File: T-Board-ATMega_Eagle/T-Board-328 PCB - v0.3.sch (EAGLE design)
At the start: 25 parts, among them IC1 LD117MIRROR, IC4 NCP1117MIRROR, J1 POWER_JACKPTH, J2 AVR_SPI_PRG_6PTH, U1 ATMEGA328P_PDIP

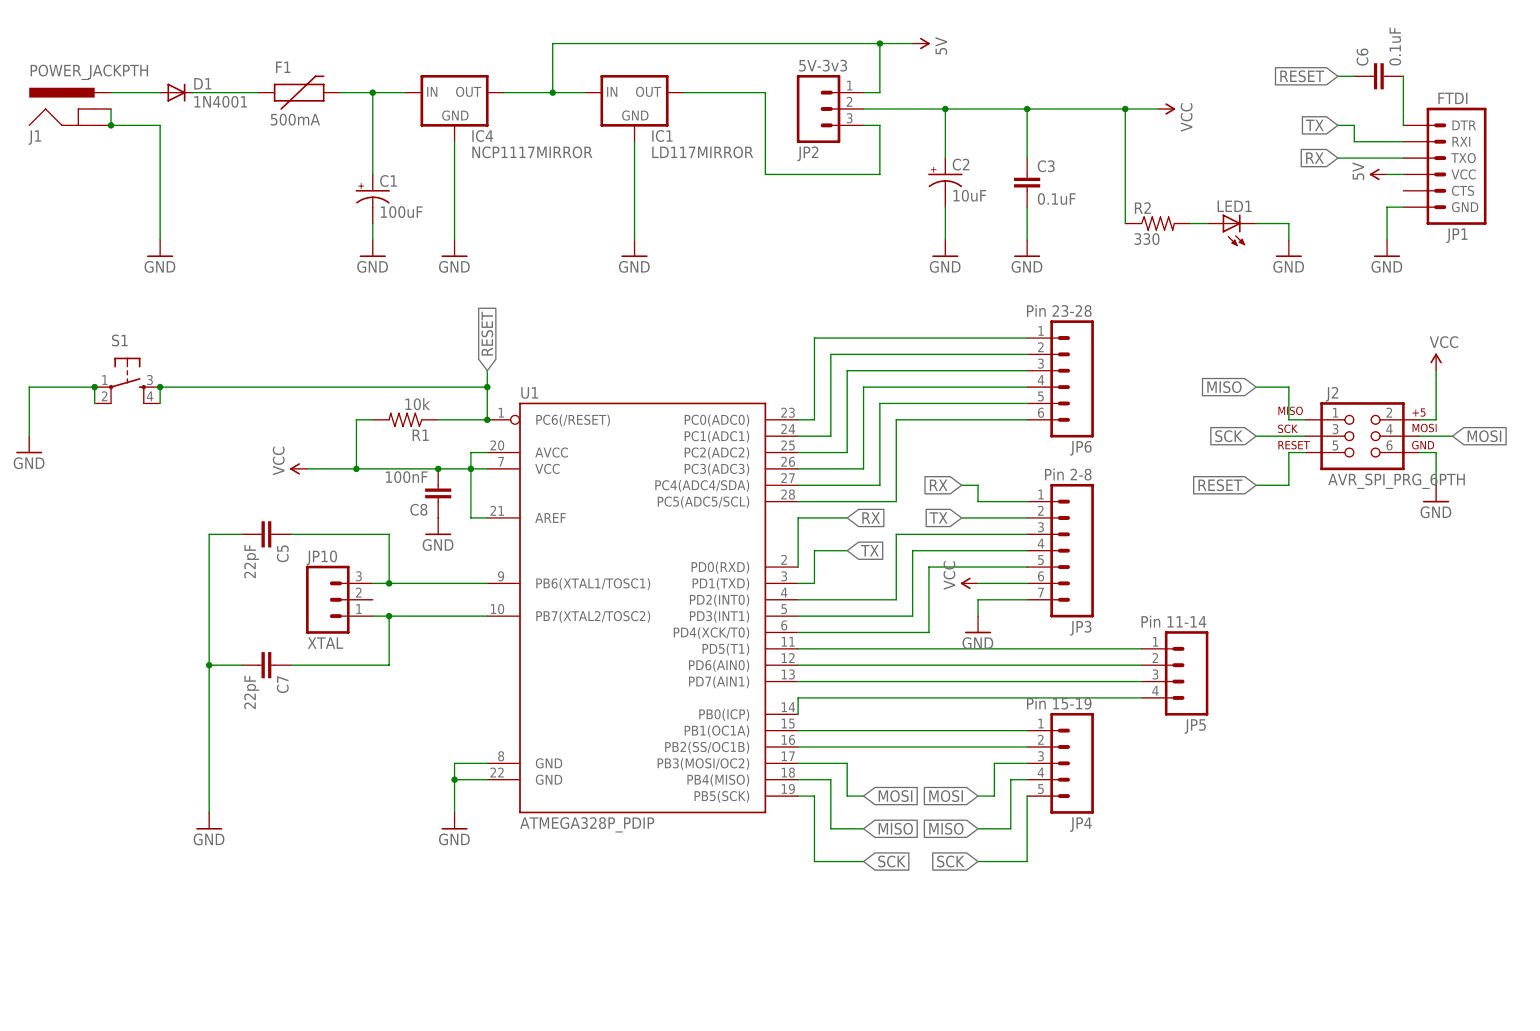
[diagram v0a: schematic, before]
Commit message: v0.4 - Second Prototype
Second prototype sent to OSHPark for fab.
- Reduced footprint
- Corrected mirrored voltage regulators
- Corrected unconnected capacitor
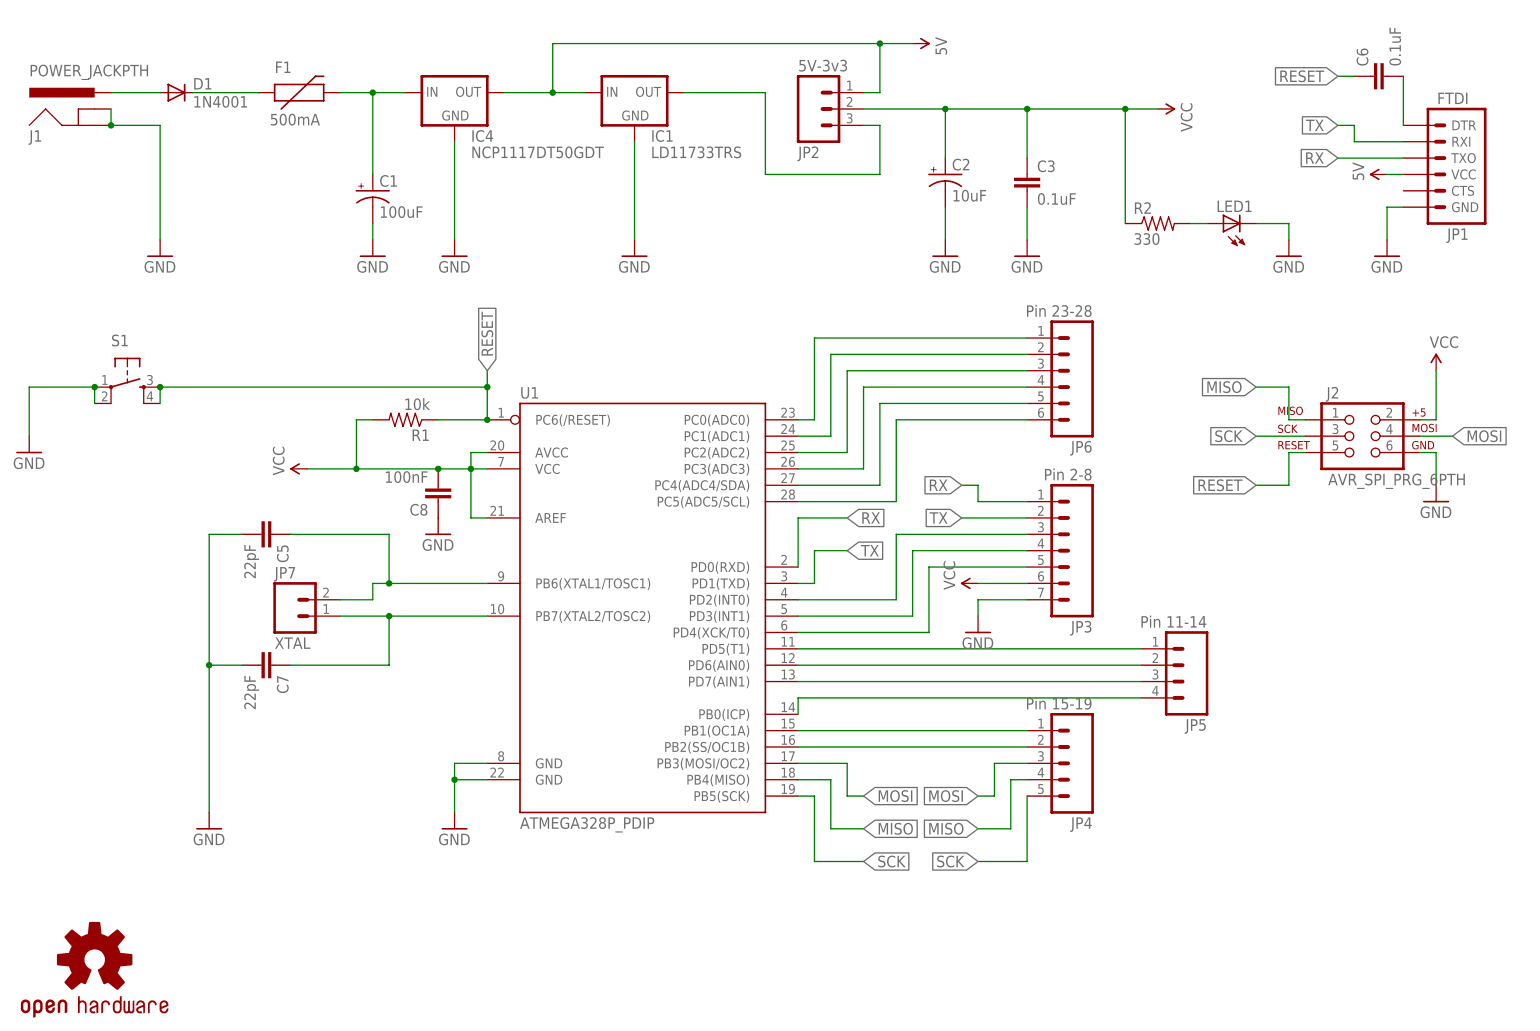
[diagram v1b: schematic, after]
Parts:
- removed JP10: XTAL, SparkFun-Connectors:M03PTH
- added JP7: XTAL, SparkFun-Connectors:M02PTH
- added LOGO1: OSHW-LOGOS, SparkFun-Aesthetics:OSHW-LOGOS
- IC1: value LD117MIRROR -> LD11733TRS; device AndyTallack:LD117MIRROR -> AndyTallack:LD11733TRS
- IC4: value NCP1117MIRROR -> NCP1117DT50GDT; device AndyTallack:NCP1117MIRROR -> AndyTallack:NCP1117DT50GDT
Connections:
- net N$7: now also JP7.1; no longer JP10.1
- net N$8: now also JP7.2; no longer JP10.3
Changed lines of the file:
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@@
 <part name="GND1" library="SparkFun-Aesthetics" deviceset="GND" device=""/>
 <part name="GND2" library="SparkFun-Aesthetics" deviceset="GND" device=""/>
-<part name="IC4" library="AndyTallack" deviceset="NCP1117" device="MIRROR" value="NCP1117MIRROR"/>
-<part name="IC1" library="AndyTallack" deviceset="LD117" device="MIRROR" value="LD117MIRROR"/>
+<part name="IC4" library="AndyTallack" deviceset="NCP1117" device="DT" technology="DT50G" value="NCP1117DT50GDT"/>
+<part name="IC1" library="AndyTallack" deviceset="LD117" device="S" technology="33TR" value="LD11733TRS"/>
 <part name="GND3" library="SparkFun-Aesthetics" deviceset="GND" device=""/>
 <part name="SUPPLY1" library="SparkFun-Aesthetics" deviceset="VCC" device=""/>
@@
 <part name="C8" library="SparkFun-Passives" deviceset="CAP" device="1206" value="100nF"/>
 <part name="SUPPLY3" library="SparkFun-Aesthetics" deviceset="5V" device=""/>
-<part name="JP10" library="SparkFun-Connectors" deviceset="M03" device="PTH" value="XTAL"/>
 <part name="LED1" library="SparkFun-LED" deviceset="LED" device="1206"/>
 <part name="GND13" library="SparkFun-Aesthetics" deviceset="GND" device=""/>
@@
 <part name="S1" library="SparkFun-Electromechanical" deviceset="TAC_SWITCH" device="PTH"/>
 <part name="GND7" library="SparkFun-Aesthetics" deviceset="GND" device=""/>
+<part name="JP7" library="SparkFun-Connectors" deviceset="M02" device="PTH" value="XTAL"/>
+<part name="LOGO1" library="SparkFun-Aesthetics" deviceset="OSHW-LOGO" device="S"/>
 </parts>
 <sheets>
@@
 <instance part="C8" gate="G$1" x="43.18" y="86.36" rot="R180"/>
 <instance part="SUPPLY3" gate="G$1" x="190.5" y="134.62" rot="R90"/>
-<instance part="JP10" gate="G$1" x="25.4" y="68.58"/>
 <instance part="LED1" gate="G$1" x="165.1" y="127" rot="R90"/>
 <instance part="GND13" gate="1" x="175.26" y="121.92"/>
@@
 <instance part="S1" gate="S" x="-5.08" y="101.6"/>
 <instance part="GND7" gate="1" x="-20.32" y="91.44"/>
+<instance part="JP7" gate="G$1" x="20.32" y="66.04"/>
+<instance part="LOGO1" gate="G$1" x="-10.16" y="12.7"/>
 </instances>
 <busses>
@@
 <segment>
 <pinref part="U1" gate="G$1" pin="PB7(XTAL2/TOSC2)"/>
-<pinref part="JP10" gate="G$1" pin="1"/>
 <wire x1="50.8" y1="66.04" x2="35.56" y2="66.04" width="0.1524" layer="91"/>
 <pinref part="C7" gate="G$1" pin="1"/>
-<wire x1="35.56" y1="66.04" x2="33.02" y2="66.04" width="0.1524" layer="91"/>
 <wire x1="35.56" y1="66.04" x2="35.56" y2="58.42" width="0.1524" layer="91"/>
 <wire x1="35.56" y1="58.42" x2="20.32" y2="58.42" width="0.1524" layer="91"/>
 <junction x="35.56" y="66.04"/>
+<pinref part="JP7" gate="G$1" pin="1"/>
+<wire x1="27.94" y1="66.04" x2="35.56" y2="66.04" width="0.1524" layer="91"/>
 </segment>
 </net>
@@
 <segment>
 <pinref part="U1" gate="G$1" pin="PB6(XTAL1/TOSC1)"/>
-<pinref part="JP10" gate="G$1" pin="3"/>
 <wire x1="50.8" y1="71.12" x2="35.56" y2="71.12" width="0.1524" layer="91"/>
 <pinref part="C5" gate="G$1" pin="1"/>
@@
 <wire x1="35.56" y1="78.74" x2="20.32" y2="78.74" width="0.1524" layer="91"/>
 <junction x="35.56" y="71.12"/>
-</segment>
-</net>
+<pinref part="JP7" gate="G$1" pin="2"/>
+<wire x1="27.94" y1="68.58" x2="33.02" y2="68.58" width="0.1524" layer="91"/>
+<wire x1="33.02" y1="68.58" x2="33.02" y2="71.12" width="0.1524" layer="91"/>
+</segment>
+</net>
